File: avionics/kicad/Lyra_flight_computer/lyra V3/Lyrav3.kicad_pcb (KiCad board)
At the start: 4 copper layers, 25 x 60 mm, 86 parts, among them J1 Screw_Terminal_01x08, J2 Screw_Terminal_01x06, J3 Conn_01x02, J4 Conn_01x02, J5 Conn_01x03, J6 Conn_01x06, J7 USB_B_Micro, J8 Conn_01x04, Q1 AO3401A, Q2 KY6802, Q3 KY6802, U2 BMI088, U3 MPL3115A2, U4 ADXL375BCCZ-RL7, U5 LIS3MDL, U6 ADS1015IDGS, U7 W25Q64JVXGIQ, U8 RP2040, U9 LDK130-33_SOT23_SOT353, X1 S3D12.288000B20F30T

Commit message: lyrav3update
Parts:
- R10, R11, R12, R13, R21, R23, R24, R25: moved to B.Cu
- moved Q3 94.2 mm to (198.9, 107.2), turned to -90 degrees
- moved Q2 93.8 mm to (199.0, 97.0), turned to -90 degrees
- moved R9 89.9 mm to (200.7, 104.8), turned to 180 degrees
- moved R11 88.9 mm to (200.7, 104.8)
- moved R13 88.2 mm to (200.7, 105.8), turned to 180 degrees
- moved R8 88.0 mm to (200.7, 94.7), turned to 180 degrees
- moved R10 87.2 mm to (200.7, 94.7)
- moved R12 86.8 mm to (200.7, 95.8), turned to 180 degrees
- moved R20 86.2 mm to (200.7, 109.5), turned to 180 degrees
- moved R23 86.0 mm to (200.7, 109.5)
- moved R19 84.3 mm to (200.5, 99.3), turned to 180 degrees
- moved R25 84.3 mm to (200.7, 108.5), turned to 180 degrees
- moved R21 83.7 mm to (200.5, 99.3)
- moved R24 82.1 mm to (200.5, 98.3), turned to 180 degrees
- moved U6 70.3 mm to (193.9, 101.3)
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
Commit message: lyrav3 work
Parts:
- removed D1: LED, LED_SMD:LED_0805_2012Metric
- removed R1: 1k, Resistor_SMD:R_0402_1005Metric
- C1, C12, C13, C14, C2, C4, R2, R3: moved to B.Cu
- moved R2 88.5 mm to (199.1, 91.9), turned to 90 degrees
- moved R7 86.1 mm to (196.7, 75.8), turned to -90 degrees
- moved R6 84.8 mm to (195.7, 75.8), turned to -90 degrees
- moved R15 83.7 mm to (200.8, 84.2), turned to 180 degrees
- moved R18 83.4 mm to (200.8, 85.2)
- moved R3 81.7 mm to (192.3, 93.7), turned to 180 degrees
- moved C10 77.5 mm to (197.6, 64.7), turned to -90 degrees
- moved C11 77.2 mm to (197.6, 67.9), turned to 90 degrees
- moved C13 75.4 mm to (201.2, 72.0), turned to 180 degrees
- moved C14 75.3 mm to (201.2, 74.0), turned to 180 degrees
- moved C12 75.1 mm to (201.2, 73.0), turned to 180 degrees
- moved C8 74.6 mm to (193.8, 107.2), turned to 180 degrees
- moved C9 73.3 mm to (194.3, 66.6), turned to 90 degrees
- moved C3 72.6 mm to (194.8, 68.5)
- moved C2 68.7 mm to (191.7, 73.7), turned to 180 degrees
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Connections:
- C29 pad 2: Net-(U9-GND) -> GND
- C5 pad 2: Net-(U9-GND) -> GND
- C6 pad 2: Net-(U9-GND) -> GND
- R6 pad 2: /I2C1 SCL -> /I2C0 SCL
- R7 pad 2: /I2C1 SDA -> /I2C0 SDA
- U6 pad 10: /I2C1 SCL -> /I2C0 SCL
- U6 pad 9: /I2C1 SDA -> /I2C0 SDA
- U9 pad 2: Net-(U9-GND) -> GND

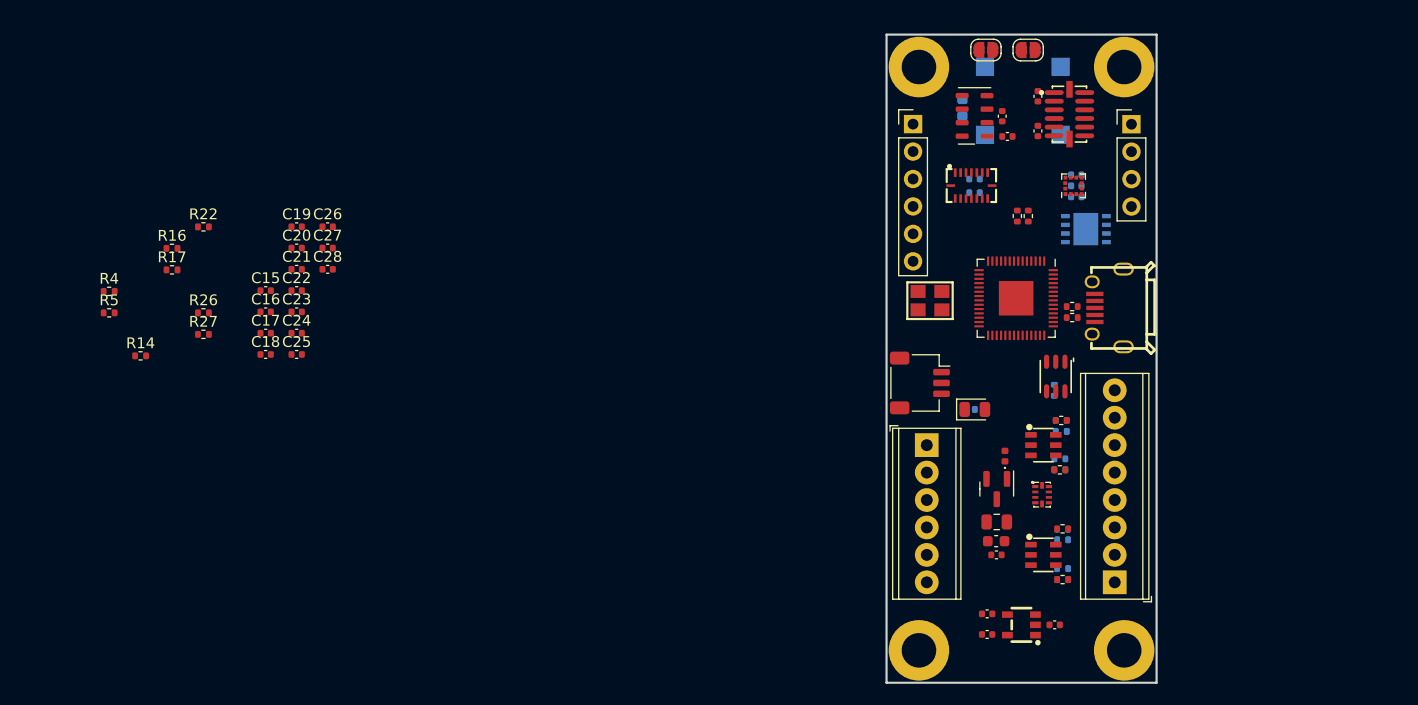
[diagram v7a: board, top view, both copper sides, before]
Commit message: more everything to back of board, find JLC components for everything
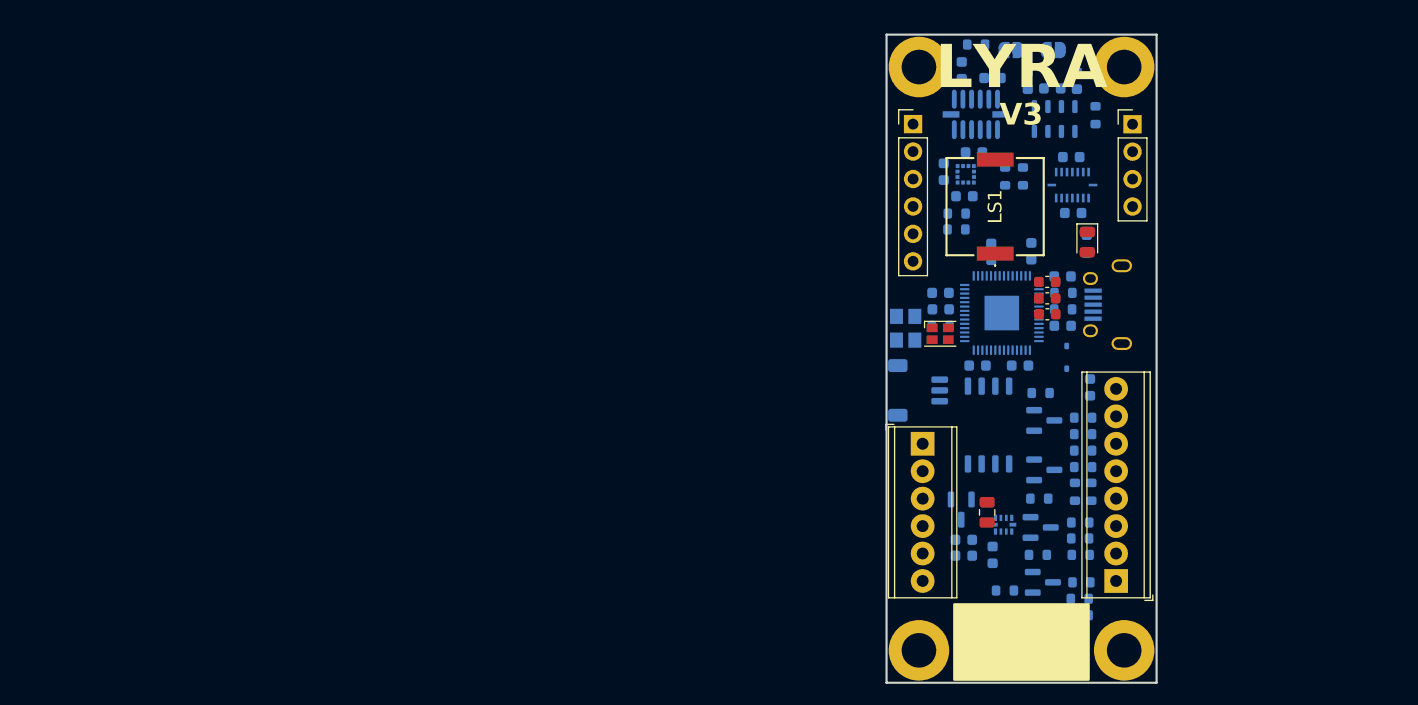
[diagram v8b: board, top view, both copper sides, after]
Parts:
- removed BUZZER1: MLT-7525, easyeda2kicad:BUZ-SMD_4P-L7.5-W7.5-P7.59-TL
- removed C27: 2u2, Capacitor_SMD:C_0402_1005Metric
- removed C29: 100n, Capacitor_SMD:C_0402_1005Metric
- removed LED1: FM-Z2727RGBA-SH, easyeda2kicad:LED-SMD_6P-L2.7-W2.8-TL
- removed R14: 10k, Resistor_SMD:R_0402_1005Metric
- removed U9: LDK130-33_SOT23_SOT353, easyeda2kicad:SOT-23-5_L3.0-W1.6-P0.95-LS2.8-BL
- added D4: LED_ARGB, customfootprints:LED_Cree-PLCC4_2x2mm_CCW, F.Cu at (188.6, 86.7)
- added LS1: PKMCS0909E4000-R1, SamacSys_Parts4:PKMCS0909E4000R1, F.Cu at (193.6, 74.9)
- added Q4: AO3400A, Package_TO_SOT_SMD:SOT-23, B.Cu at (197.9, 104.6)
- added Q5: AO3400A, Package_TO_SOT_SMD:SOT-23, B.Cu at (198.1, 109.7)
- added R1: 6k, Resistor_SMD:R_0603_1608Metric, B.Cu at (191.9, 59.9)
- added U1: AZ1117-3.3, Package_TO_SOT_SMD:SOT-223, B.Cu at (194.3, 115.3)
- C1, C12, C13, C14, C18, C19, C2, C20: footprint Capacitor_SMD:C_0402_1005Metric -> Capacitor_SMD:C_0603_1608Metric
- C10, C11, C15, C16, C17, C21, C22, C23, C24, C25, C26, C28, C3, C8, C9: footprint Capacitor_SMD:C_0402_1005Metric -> Capacitor_SMD:C_0603_1608Metric; moved to B.Cu
- C5, C6: value 1u -> 10u; footprint Capacitor_SMD:C_0402_1005Metric -> Capacitor_SMD:C_0603_1608Metric; moved to B.Cu
- C7, J3, J4, J5, J7, Q1, U2, U3, U4, U5, U6, U8, X1: moved to B.Cu
- D3: footprint Diode_SMD:D_0402_1005Metric -> Diode_SMD:D_SOD-323; moved to B.Cu
- Q2, Q3: value KY6802 -> AO3400A; footprint easyeda2kicad:SOT-23-6_L2.9-W1.6-P0.95-LS2.8-BL -> Package_TO_SOT_SMD:SOT-23; moved to B.Cu
- R10, R11, R12, R13, R2, R21, R23, R24, R25, R3: footprint Resistor_SMD:R_0402_1005Metric -> Resistor_SMD:R_0603_1608Metric
- R15, R18, R19, R20, R22, R4, R5, R6, R7, R8, R9: footprint Resistor_SMD:R_0402_1005Metric -> Resistor_SMD:R_0603_1608Metric; moved to B.Cu
- R16, R17, R26, R27: value 470R -> 1k; footprint Resistor_SMD:R_0402_1005Metric -> Resistor_SMD:R_0603_1608Metric; moved to B.Cu
- U7: value W25Q64JVXGIQ -> W25Q64JVXGIQ; footprint easyeda2kicad:XSON-8_L4.0-W4.0-P0.80-TL-EP -> Package_SO:SOIC-8_5.23x5.23mm_P1.27mm
- moved R17 84.4 mm to (197.6, 107.2), turned to 180 degrees
- moved R22 83.2 mm to (202.9, 66.5), turned to 90 degrees
- moved R16 81.5 mm to (197.9, 92.2), turned to 180 degrees
- moved R26 79.3 mm to (197.7, 102.0), turned to 180 degrees
- moved R5 78.8 mm to (190.1, 77.1), turned to 180 degrees
- moved R4 78.8 mm to (190.1, 75.6)
- moved R27 77.9 mm to (194.6, 110.5)
- moved C17 73.8 mm to (199.9, 86.0)
- moved C18 72.5 mm to (198.5, 83.4)
- moved C15 71.6 mm to (193.4, 107.2), turned to -90 degrees
- moved C28 71.4 mm to (202.4, 91.7), turned to 90 degrees
- moved C25 71.3 mm to (199.9, 81.4)
- moved C20 69.8 mm to (198.5, 84.9)
- moved C19 69.7 mm to (198.5, 81.9)
- moved C21 68.0 mm to (197.0, 79.1), turned to 90 degrees
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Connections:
- J6 pad 1: /BRKOUT5 -> /BRKOUT7
- J6 pad 3: /BRKOUT7 -> /BRKOUT5
- J8 pad 1: /BRKOUT4 -> /BRKOUT1
- J8 pad 2: /BRKOUT3 -> /BRKOUT2
- J8 pad 3: /BRKOUT2 -> /BRKOUT3
- J8 pad 4: /BRKOUT1 -> /BRKOUT4
- Q2 pad 1: /P1 EN  -> /P2 EN 
- Q2 pad 3: /P2 EN  -> Net-(Q2-D)
- Q3 pad 1: /P3 EN  -> /P1 EN 
- Q3 pad 3: /P4 EN  -> Net-(Q3-D)
- R10 pad 1: Net-(Q2A-D) -> Net-(Q3-D)
- R11 pad 1: Net-(Q3A-D) -> Net-(Q4-D)
- R19 pad 2: Net-(Q2B-D) -> Net-(Q2-D)
- R20 pad 2: Net-(Q3B-D) -> Net-(Q5-D)
- R21 pad 1: Net-(Q2B-D) -> Net-(Q2-D)
- R23 pad 1: Net-(Q3B-D) -> Net-(Q5-D)
- R4 pad 1: +12V -> +12VA
- R8 pad 2: Net-(Q2A-D) -> Net-(Q3-D)
- R9 pad 2: Net-(Q3A-D) -> Net-(Q4-D)
- U8 pad 15: unconnected-(U8-GPIO12-Pad15) -> /LEDRED
- U8 pad 16: /BRKOUT5 -> /LEDGREEN
- U8 pad 17: /BRKOUT6 -> /LEDBLUE
- U8 pad 18: /BRKOUT7 -> unconnected-(U8-GPIO15-Pad18)
- U8 pad 2: /BRKOUT1 -> unconnected-(U8-GPIO0-Pad2)
- U8 pad 27: unconnected-(U8-GPIO16-Pad27) -> /BRKOUT5
- U8 pad 28: unconnected-(U8-GPIO17-Pad28) -> /BRKOUT6
- U8 pad 29: unconnected-(U8-GPIO18-Pad29) -> /BRKOUT7
- U8 pad 3: /BRKOUT2 -> unconnected-(U8-GPIO1-Pad3)
- U8 pad 34: unconnected-(U8-GPIO22-Pad34) -> /BUZZER
- U8 pad 35: /LEDRED -> unconnected-(U8-GPIO23-Pad35)
- U8 pad 36: /LEDGREEN -> unconnected-(U8-GPIO24-Pad36)
- U8 pad 37: /LEDBLUE -> /BRKOUT1
- U8 pad 38: unconnected-(U8-GPIO26_ADC0-Pad38) -> /BATT SENSE 
- U8 pad 39: unconnected-(U8-GPIO27_ADC1-Pad39) -> /BRKOUT2
- U8 pad 4: /BRKOUT3 -> unconnected-(U8-GPIO2-Pad4)
- U8 pad 40: /BATT SENSE  -> /BRKOUT3
- U8 pad 41: unconnected-(U8-GPIO29_ADC3-Pad41) -> /BRKOUT4
- U8 pad 5: /BRKOUT4 -> unconnected-(U8-GPIO3-Pad5)
- U8 pad 8: /BUZZER -> unconnected-(U8-GPIO6-Pad8)
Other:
- board text added: "LYRA"
- board text added: "V3"
